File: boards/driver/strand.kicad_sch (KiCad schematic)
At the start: 8 parts, among them Q26 MMBT2222, Q27 MMBT2907

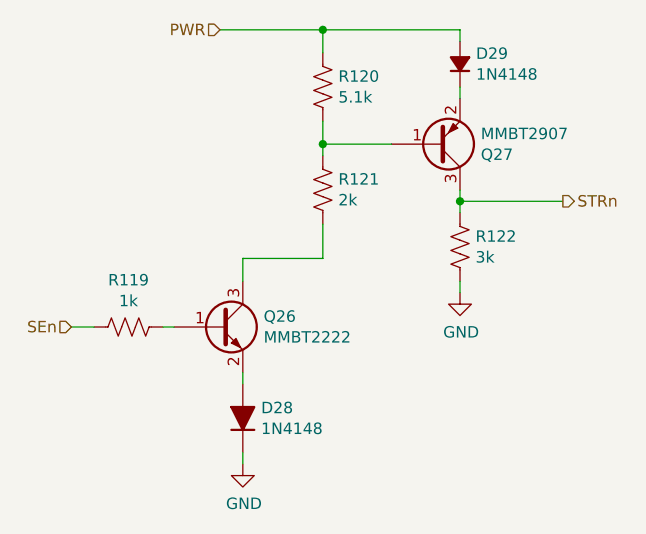
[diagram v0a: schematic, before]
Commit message: Driver: Added a 5V->3.3V LDO to replace the reversed cmod header, added jumpers for the 200R parallel returns, and renamed subcircuit ports to avoid unexpected ground connections.
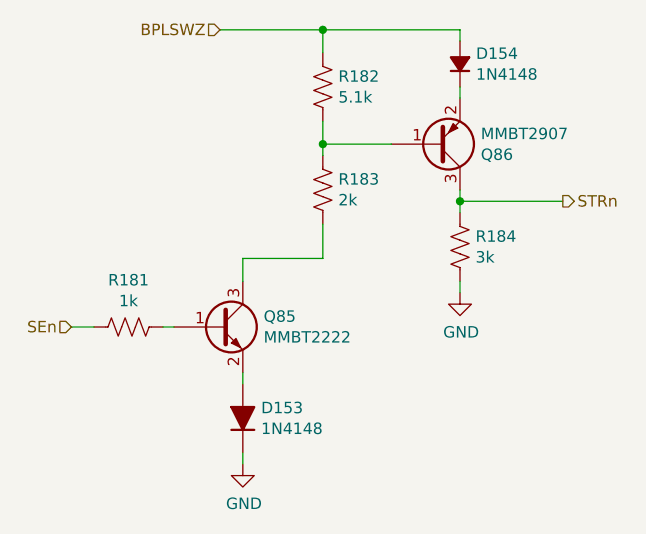
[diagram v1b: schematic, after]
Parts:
- renumbered D28 to D153, D29 to D154, Q26 to Q85, Q27 to Q86, R119 to R181, R120 to R182, R121 to R183, R122 to R184
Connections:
- net PWR renamed BPLSWZ
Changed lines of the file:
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@@
     (effects (font (size 1.27 1.27)) (justify right))
   )
-  (hierarchical_label "PWR" (shape input) (at 130.81 69.85 180)
+  (hierarchical_label "BPLSWZ" (shape input) (at 130.81 69.85 180)
     (effects (font (size 1.27 1.27)) (justify right))
   )
   (symbol (lib_id "power:GND") (at 157.48 99.06 0)
     (in_bom yes) (on_board yes)
-    (property "Reference" "#PWR082" (id 0) (at 157.48 105.41 0)
+    (property "Reference" "#PWR072" (id 0) (at 157.48 105.41 0)
       (effects (font (size 1.27 1.27)) hide)
     )
@@
   (symbol (lib_id "Device:R_US") (at 142.24 87.63 0)
     (in_bom yes) (on_board yes)
-    (property "Reference" "R121" (id 0) (at 143.9672 86.4616 0)
+    (property "Reference" "R183" (id 0) (at 143.9672 86.4616 0)
       (effects (font (size 1.27 1.27)) (justify left))
     )
@@
   (symbol (lib_id "Device:R_US") (at 142.24 76.2 0)
     (in_bom yes) (on_board yes)
-    (property "Reference" "R120" (id 0) (at 143.9672 75.0316 0)
+    (property "Reference" "R182" (id 0) (at 143.9672 75.0316 0)
       (effects (font (size 1.27 1.27)) (justify left))
     )
@@
   (symbol (lib_id "Device:Q_PNP_BEC") (at 154.94 82.55 0) (mirror x)
     (in_bom yes) (on_board yes)
-    (property "Reference" "Q27" (id 0) (at 159.7914 83.7184 0)
+    (property "Reference" "Q86" (id 0) (at 159.7914 83.7184 0)
       (effects (font (size 1.27 1.27)) (justify left))
     )
@@
   (symbol (lib_id "Device:R_US") (at 157.48 93.98 0)
     (in_bom yes) (on_board yes)
-    (property "Reference" "R122" (id 0) (at 159.2072 92.8116 0)
+    (property "Reference" "R184" (id 0) (at 159.2072 92.8116 0)
       (effects (font (size 1.27 1.27)) (justify left))
     )
@@
   (symbol (lib_id "Device:D_Small_Filled") (at 157.48 73.66 90)
     (in_bom yes) (on_board yes)
-    (property "Reference" "D29" (id 0) (at 159.258 72.4916 90)
+    (property "Reference" "D154" (id 0) (at 159.258 72.4916 90)
       (effects (font (size 1.27 1.27)) (justify right))
     )
@@
   (symbol (lib_id "Device:R_US") (at 120.65 102.87 270)
     (in_bom yes) (on_board yes)
-    (property "Reference" "R119" (id 0) (at 120.65 97.663 90))
+    (property "Reference" "R181" (id 0) (at 120.65 97.663 90))
     (property "Value" "1k" (id 1) (at 120.65 99.9744 90))
     (property "Footprint" "Resistor_SMD:R_0603_1608Metric" (id 2) (at 120.396 103.886 90)
@@
   (symbol (lib_id "Device:Q_NPN_BEC") (at 130.81 102.87 0)
     (in_bom yes) (on_board yes)
-    (property "Reference" "Q26" (id 0) (at 135.6614 101.7016 0)
+    (property "Reference" "Q85" (id 0) (at 135.6614 101.7016 0)
       (effects (font (size 1.27 1.27)) (justify left))
     )
@@
   (symbol (lib_id "Device:D_Filled") (at 133.35 113.03 90)
     (in_bom yes) (on_board yes)
-    (property "Reference" "D28" (id 0) (at 135.382 111.8616 90)
+    (property "Reference" "D153" (id 0) (at 135.382 111.8616 90)
       (effects (font (size 1.27 1.27)) (justify right))
     )
@@
   (symbol (lib_id "power:GND") (at 133.35 118.11 0)
     (in_bom yes) (on_board yes)
-    (property "Reference" "#PWR081" (id 0) (at 133.35 124.46 0)
+    (property "Reference" "#PWR071" (id 0) (at 133.35 124.46 0)
       (effects (font (size 1.27 1.27)) hide)
     )

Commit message: Driver: incorporated most changes from the test board, and began layout
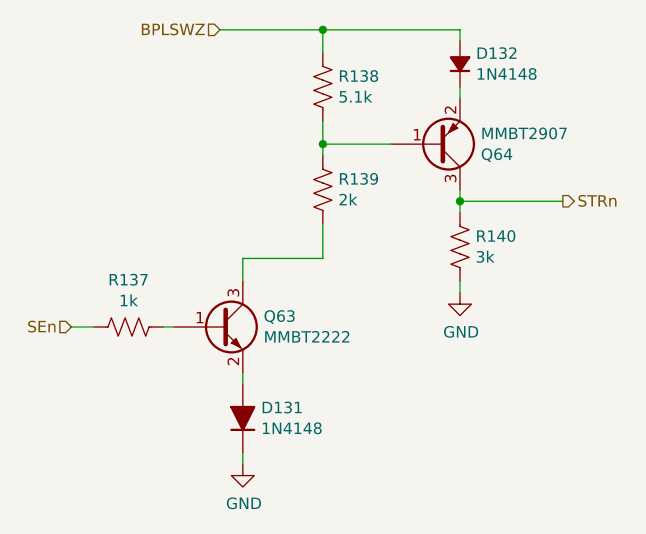
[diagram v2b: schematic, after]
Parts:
- D131: renamed from D153; footprint Diode_SMD:D_SOD-323 -> lachesis:D_SOD-323
- D132: renamed from D154; footprint Diode_SMD:D_SOD-323 -> lachesis:D_SOD-323
- renumbered Q85 to Q63, Q86 to Q64, R181 to R137, R182 to R138, R183 to R139, R184 to R140
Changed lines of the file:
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@@
     (effects (font (size 1.27 1.27)) (justify right))
   )
-  (symbol (lib_id "power:GND") (at 157.48 99.06 0)
+  (symbol (lib_id "power:GND") (at 157.48 99.06 0) (unit 1)
     (in_bom yes) (on_board yes)
-    (property "Reference" "#PWR072" (id 0) (at 157.48 105.41 0)
+    (property "Reference" "#PWR050" (id 0) (at 157.48 105.41 0)
       (effects (font (size 1.27 1.27)) hide)
     )
@@
     (pin "1")
   )
-  (symbol (lib_id "Device:R_US") (at 142.24 87.63 0)
+  (symbol (lib_id "Device:R_US") (at 142.24 87.63 0) (unit 1)
     (in_bom yes) (on_board yes)
-    (property "Reference" "R183" (id 0) (at 143.9672 86.4616 0)
+    (property "Reference" "R139" (id 0) (at 143.9672 86.4616 0)
       (effects (font (size 1.27 1.27)) (justify left))
     )
@@
     (pin "2")
   )
-  (symbol (lib_id "Device:R_US") (at 142.24 76.2 0)
+  (symbol (lib_id "Device:R_US") (at 142.24 76.2 0) (unit 1)
     (in_bom yes) (on_board yes)
-    (property "Reference" "R182" (id 0) (at 143.9672 75.0316 0)
+    (property "Reference" "R138" (id 0) (at 143.9672 75.0316 0)
       (effects (font (size 1.27 1.27)) (justify left))
     )
@@
     (pin "2")
   )
-  (symbol (lib_id "Device:Q_PNP_BEC") (at 154.94 82.55 0) (mirror x)
+  (symbol (lib_id "Device:Q_PNP_BEC") (at 154.94 82.55 0) (mirror x) (unit 1)
     (in_bom yes) (on_board yes)
-    (property "Reference" "Q86" (id 0) (at 159.7914 83.7184 0)
+    (property "Reference" "Q64" (id 0) (at 159.7914 83.7184 0)
       (effects (font (size 1.27 1.27)) (justify left))
     )
@@
     (pin "3")
   )
-  (symbol (lib_id "Device:R_US") (at 157.48 93.98 0)
+  (symbol (lib_id "Device:R_US") (at 157.48 93.98 0) (unit 1)
     (in_bom yes) (on_board yes)
-    (property "Reference" "R184" (id 0) (at 159.2072 92.8116 0)
+    (property "Reference" "R140" (id 0) (at 159.2072 92.8116 0)
       (effects (font (size 1.27 1.27)) (justify left))
     )
@@
     (pin "2")
   )
-  (symbol (lib_id "Device:D_Small_Filled") (at 157.48 73.66 90)
+  (symbol (lib_id "Device:D_Small_Filled") (at 157.48 73.66 90) (unit 1)
     (in_bom yes) (on_board yes)
-    (property "Reference" "D154" (id 0) (at 159.258 72.4916 90)
+    (property "Reference" "D132" (id 0) (at 159.258 72.4916 90)
       (effects (font (size 1.27 1.27)) (justify right))
     )
@@
       (effects (font (size 1.27 1.27)) (justify right))
     )
-    (property "Footprint" "Diode_SMD:D_SOD-323" (id 2) (at 157.48 73.66 90)
+    (property "Footprint" "lachesis:D_SOD-323" (id 2) (at 157.48 73.66 90)
       (effects (font (size 1.27 1.27)) hide)
     )
@@
     (pin "2")
   )
-  (symbol (lib_id "Device:R_US") (at 120.65 102.87 270)
+  (symbol (lib_id "Device:R_US") (at 120.65 102.87 270) (unit 1)
     (in_bom yes) (on_board yes)
-    (property "Reference" "R181" (id 0) (at 120.65 97.663 90))
+    (property "Reference" "R137" (id 0) (at 120.65 97.663 90))
     (property "Value" "1k" (id 1) (at 120.65 99.9744 90))
     (property "Footprint" "Resistor_SMD:R_0603_1608Metric" (id 2) (at 120.396 103.886 90)
@@
     (pin "2")
   )
-  (symbol (lib_id "Device:Q_NPN_BEC") (at 130.81 102.87 0)
+  (symbol (lib_id "Device:Q_NPN_BEC") (at 130.81 102.87 0) (unit 1)
     (in_bom yes) (on_board yes)
-    (property "Reference" "Q85" (id 0) (at 135.6614 101.7016 0)
+    (property "Reference" "Q63" (id 0) (at 135.6614 101.7016 0)
       (effects (font (size 1.27 1.27)) (justify left))
     )
@@
     (pin "3")
   )
-  (symbol (lib_id "Device:D_Filled") (at 133.35 113.03 90)
+  (symbol (lib_id "Device:D_Filled") (at 133.35 113.03 90) (unit 1)
     (in_bom yes) (on_board yes)
-    (property "Reference" "D153" (id 0) (at 135.382 111.8616 90)
+    (property "Reference" "D131" (id 0) (at 135.382 111.8616 90)
       (effects (font (size 1.27 1.27)) (justify right))
     )
@@
       (effects (font (size 1.27 1.27)) (justify right))
     )
-    (property "Footprint" "Diode_SMD:D_SOD-323" (id 2) (at 133.35 113.03 0)
+    (property "Footprint" "lachesis:D_SOD-323" (id 2) (at 133.35 113.03 0)
       (effects (font (size 1.27 1.27)) hide)
     )
@@
     (pin "2")
   )
-  (symbol (lib_id "power:GND") (at 133.35 118.11 0)
+  (symbol (lib_id "power:GND") (at 133.35 118.11 0) (unit 1)
     (in_bom yes) (on_board yes)
-    (property "Reference" "#PWR071" (id 0) (at 133.35 124.46 0)
+    (property "Reference" "#PWR049" (id 0) (at 133.35 124.46 0)
       (effects (font (size 1.27 1.27)) hide)
     )

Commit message: Driver: minor schematic cleanup and populated all of the BOM except for resistors
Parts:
- D131, D132: MPN (none) -> 1N4148WS; Manufacturer (none) -> SMC Diode Solutions; Package (none) -> SOD-323; Rating (none) -> 300mA
- Q63: MPN (none) -> MMBT2222ALT1HTSA1; Manufacturer (none) -> Infineon Technologies; Package (none) -> SOT-23-3
- Q64: MPN (none) -> MMBT2907ALT1HTSA1; Manufacturer (none) -> Infineon Technologies; Package (none) -> SOT-23-3
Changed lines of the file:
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@@
+      (effects (font (size 1.27 1.27)) hide)
+    )
+    (property "MPN" "MMBT2907ALT1HTSA1" (id 6) (at 154.94 82.55 0)
+      (effects (font (size 1.27 1.27)) hide)
+    )
+    (property "Manufacturer" "Infineon Technologies" (id 7) (at 154.94 82.55 0)
+      (effects (font (size 1.27 1.27)) hide)
+    )
+    (property "Description" "TRANS PNP 60V 0.6A SOT23" (id 8) (at 154.94 82.55 0)
+      (effects (font (size 1.27 1.27)) hide)
+    )
+    (property "Package" "SOT-23-3" (id 9) (at 154.94 82.55 0)
       (effects (font (size 1.27 1.27)) hide)
     )
@@
       (effects (font (size 1.27 1.27)) hide)
     )
+    (property "MPN" "1N4148WS" (id 6) (at 157.48 73.66 0)
+      (effects (font (size 1.27 1.27)) hide)
+    )
+    (property "Manufacturer" "SMC Diode Solutions" (id 7) (at 157.48 73.66 0)
+      (effects (font (size 1.27 1.27)) hide)
+    )
+    (property "Description" "DIODE GEN PURP 75V 300MA SOD323" (id 8) (at 157.48 73.66 0)
+      (effects (font (size 1.27 1.27)) hide)
+    )
+    (property "Package" "SOD-323" (id 9) (at 157.48 73.66 0)
+      (effects (font (size 1.27 1.27)) hide)
+    )
+    (property "Rating" "300mA" (id 10) (at 157.48 73.66 0)
+      (effects (font (size 1.27 1.27)) hide)
+    )
     (pin "1")
     (pin "2")
@@
       (effects (font (size 1.27 1.27)) hide)
     )
+    (property "MPN" "MMBT2222ALT1HTSA1" (id 6) (at 130.81 102.87 0)
+      (effects (font (size 1.27 1.27)) hide)
+    )
+    (property "Manufacturer" "Infineon Technologies" (id 7) (at 130.81 102.87 0)
+      (effects (font (size 1.27 1.27)) hide)
+    )
+    (property "Description" "TRANS NPN 40V 0.6A SOT-23" (id 8) (at 130.81 102.87 0)
+      (effects (font (size 1.27 1.27)) hide)
+    )
+    (property "Package" "SOT-23-3" (id 9) (at 130.81 102.87 0)
+      (effects (font (size 1.27 1.27)) hide)
+    )
     (pin "1")
     (pin "2")
@@
       (effects (font (size 1.27 1.27)) hide)
     )
+    (property "MPN" "1N4148WS" (id 6) (at 133.35 113.03 0)
+      (effects (font (size 1.27 1.27)) hide)
+    )
+    (property "Manufacturer" "SMC Diode Solutions" (id 7) (at 133.35 113.03 0)
+      (effects (font (size 1.27 1.27)) hide)
+    )
+    (property "Description" "DIODE GEN PURP 75V 300MA SOD323" (id 8) (at 133.35 113.03 0)
+      (effects (font (size 1.27 1.27)) hide)
+    )
+    (property "Package" "SOD-323" (id 9) (at 133.35 113.03 0)
+      (effects (font (size 1.27 1.27)) hide)
+    )
+    (property "Rating" "300mA" (id 10) (at 133.35 113.03 0)
+      (effects (font (size 1.27 1.27)) hide)
+    )

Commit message: Driver: filled out the rest of the BOM, except for defaults for nominal resistances
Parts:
- R137: MPN (none) -> ESR03EZPF1001; Manufacturer (none) -> Rohm Semiconductor; Package (none) -> 0603; Rating (none) -> 1/4W; Tolerance (none) -> 1%
- R138: MPN (none) -> ERJ-UP3F5101V; Manufacturer (none) -> Panasonic Electronic Components; Package (none) -> 0603; Rating (none) -> 1/4W; Tolerance (none) -> 1%
- R139: MPN (none) -> ERJ-PA3F2001V; Manufacturer (none) -> Panasonic Electronic Components; Package (none) -> 0603; Rating (none) -> 1/3W; Tolerance (none) -> 1%
- R140: MPN (none) -> ERJ-PA3F3001V; Manufacturer (none) -> Panasonic Electronic Components; Package (none) -> 0603; Rating (none) -> 1/3W; Tolerance (none) -> 1%
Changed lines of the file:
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@@
+      (effects (font (size 1.27 1.27)) hide)
+    )
+    (property "Description" "RES SMD 2K OHM PULSE-WITHSTANDING 1% 1/3W 0603" (id 4) (at 142.24 87.63 0)
+      (effects (font (size 1.27 1.27)) hide)
+    )
+    (property "MPN" "ERJ-PA3F2001V" (id 5) (at 142.24 87.63 0)
+      (effects (font (size 1.27 1.27)) hide)
+    )
+    (property "Manufacturer" "Panasonic Electronic Components" (id 6) (at 142.24 87.63 0)
+      (effects (font (size 1.27 1.27)) hide)
+    )
+    (property "Package" "0603" (id 7) (at 142.24 87.63 0)
+      (effects (font (size 1.27 1.27)) hide)
+    )
+    (property "Rating" "1/3W" (id 8) (at 142.24 87.63 0)
+      (effects (font (size 1.27 1.27)) hide)
+    )
+    (property "Tolerance" "1%" (id 9) (at 142.24 87.63 0)
       (effects (font (size 1.27 1.27)) hide)
     )
@@
     )
     (property "Datasheet" "~" (id 3) (at 142.24 76.2 0)
+      (effects (font (size 1.27 1.27)) hide)
+    )
+    (property "Description" "RES 5.1K OHM PULSE-WITHSTANDING 1% 1/4W 0603" (id 4) (at 142.24 76.2 0)
+      (effects (font (size 1.27 1.27)) hide)
+    )
+    (property "MPN" "ERJ-UP3F5101V" (id 5) (at 142.24 76.2 0)
+      (effects (font (size 1.27 1.27)) hide)
+    )
+    (property "Manufacturer" "Panasonic Electronic Components" (id 6) (at 142.24 76.2 0)
+      (effects (font (size 1.27 1.27)) hide)
+    )
+    (property "Package" "0603" (id 7) (at 142.24 76.2 0)
+      (effects (font (size 1.27 1.27)) hide)
+    )
+    (property "Rating" "1/4W" (id 8) (at 142.24 76.2 0)
+      (effects (font (size 1.27 1.27)) hide)
+    )
+    (property "Tolerance" "1%" (id 9) (at 142.24 76.2 0)
       (effects (font (size 1.27 1.27)) hide)
     )
@@
       (effects (font (size 1.27 1.27)) hide)
     )
+    (property "Rating" "1/3W" (id 4) (at 157.48 93.98 0)
+      (effects (font (size 1.27 1.27)) hide)
+    )
+    (property "Tolerance" "1%" (id 5) (at 157.48 93.98 0)
+      (effects (font (size 1.27 1.27)) hide)
+    )
+    (property "Description" "RES SMD 3K OHM PULSE-WITHSTANDING 1% 1/3W 0603" (id 6) (at 157.48 93.98 0)
+      (effects (font (size 1.27 1.27)) hide)
+    )
+    (property "MPN" "ERJ-PA3F3001V" (id 7) (at 157.48 93.98 0)
+      (effects (font (size 1.27 1.27)) hide)
+    )
+    (property "Manufacturer" "Panasonic Electronic Components" (id 8) (at 157.48 93.98 0)
+      (effects (font (size 1.27 1.27)) hide)
+    )
+    (property "Package" "0603" (id 9) (at 157.48 93.98 0)
+      (effects (font (size 1.27 1.27)) hide)
+    )
     (pin "1")
     (pin "2")
@@
       (effects (font (size 1.27 1.27)) hide)
     )
+    (property "Description" "RES SMD 1K OHM PULSE-WITHSTANDING 1% 1/4W 0603" (id 4) (at 120.65 102.87 0)
+      (effects (font (size 1.27 1.27)) hide)
+    )
+    (property "MPN" "ESR03EZPF1001" (id 5) (at 120.65 102.87 0)
+      (effects (font (size 1.27 1.27)) hide)
+    )
+    (property "Manufacturer" "Rohm Semiconductor" (id 6) (at 120.65 102.87 0)
+      (effects (font (size 1.27 1.27)) hide)
+    )
+    (property "Package" "0603" (id 7) (at 120.65 102.87 0)
+      (effects (font (size 1.27 1.27)) hide)
+    )
+    (property "Rating" "1/4W" (id 8) (at 120.65 102.87 0)
+      (effects (font (size 1.27 1.27)) hide)
+    )
+    (property "Tolerance" "1%" (id 9) (at 120.65 102.87 0)
+      (effects (font (size 1.27 1.27)) hide)
+    )
